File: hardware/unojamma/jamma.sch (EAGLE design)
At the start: 21 parts, among them T1 2N3904, T2 2N3904, T3 2N3904, X1 53048-09

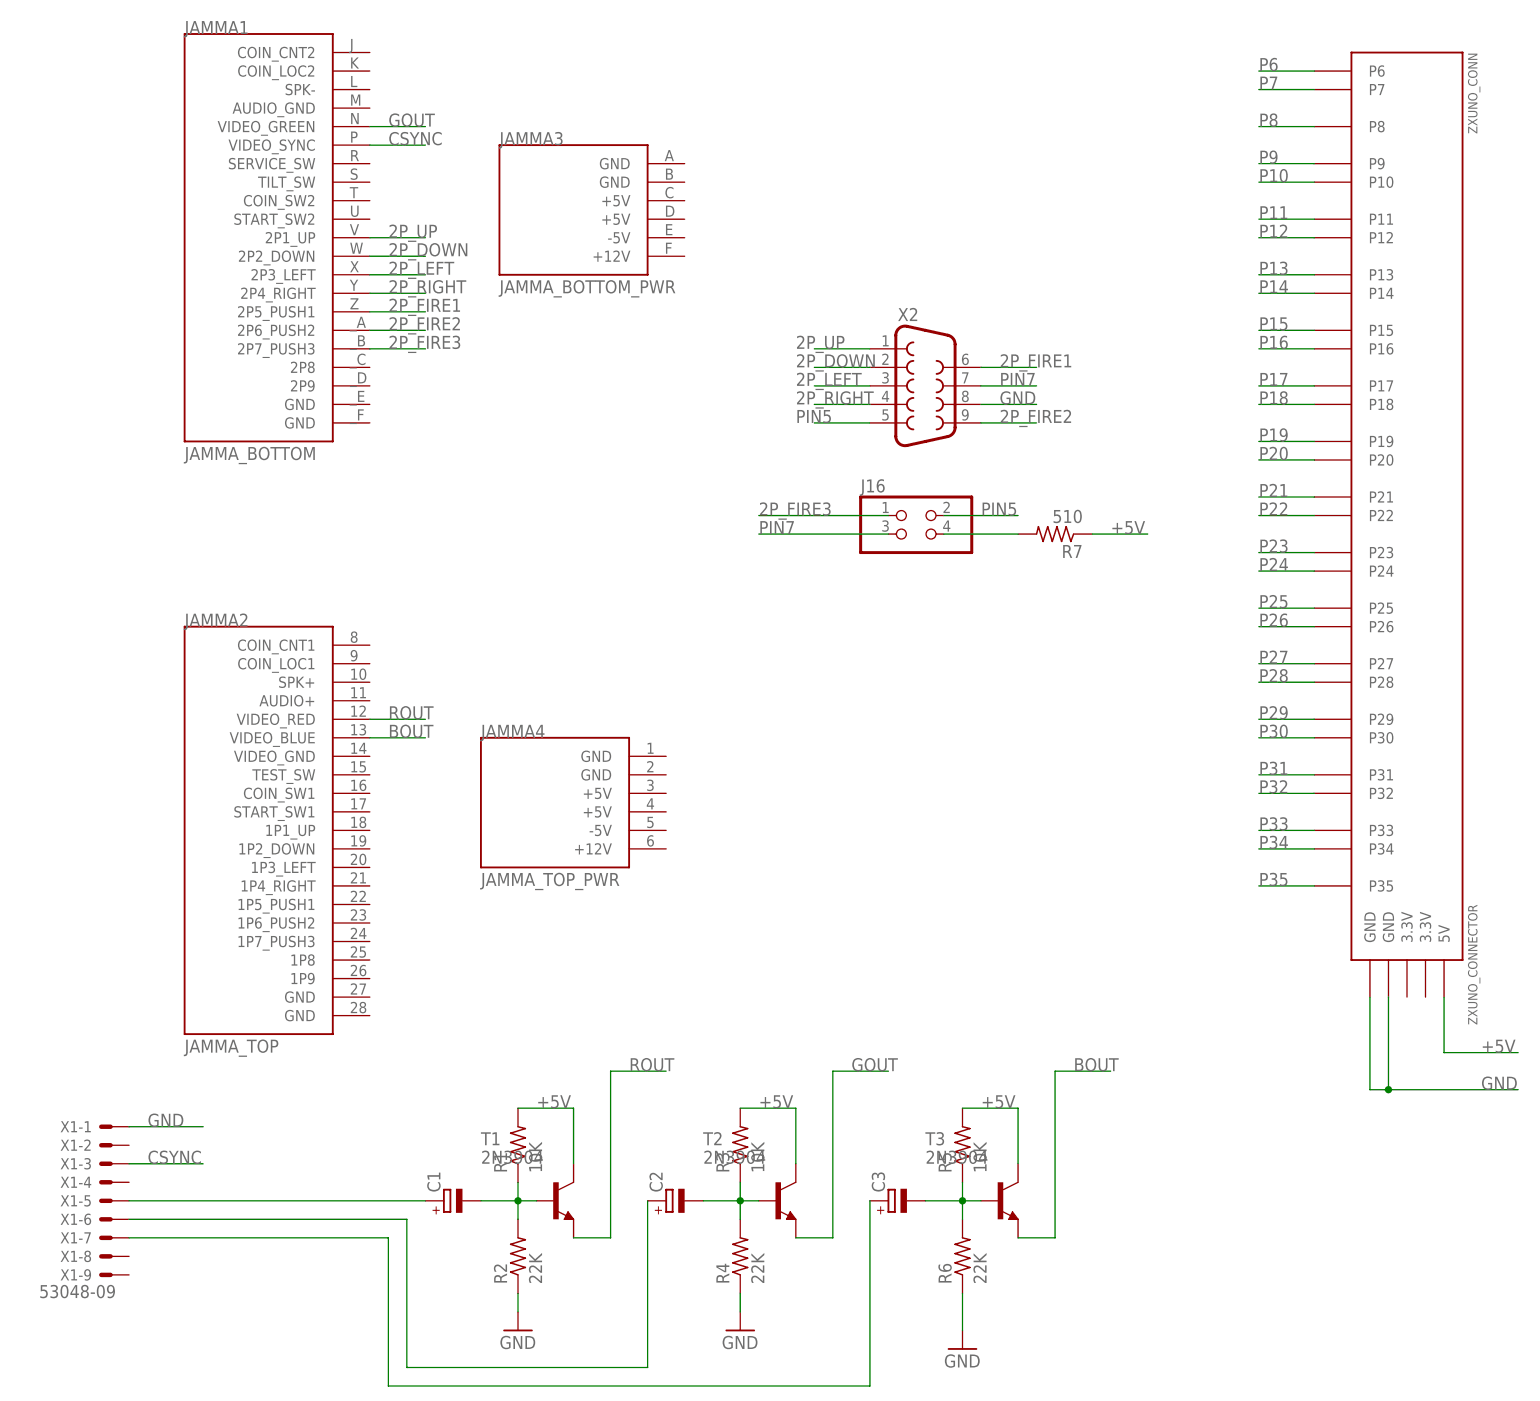
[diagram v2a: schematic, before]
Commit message: Añado amplificador de audio
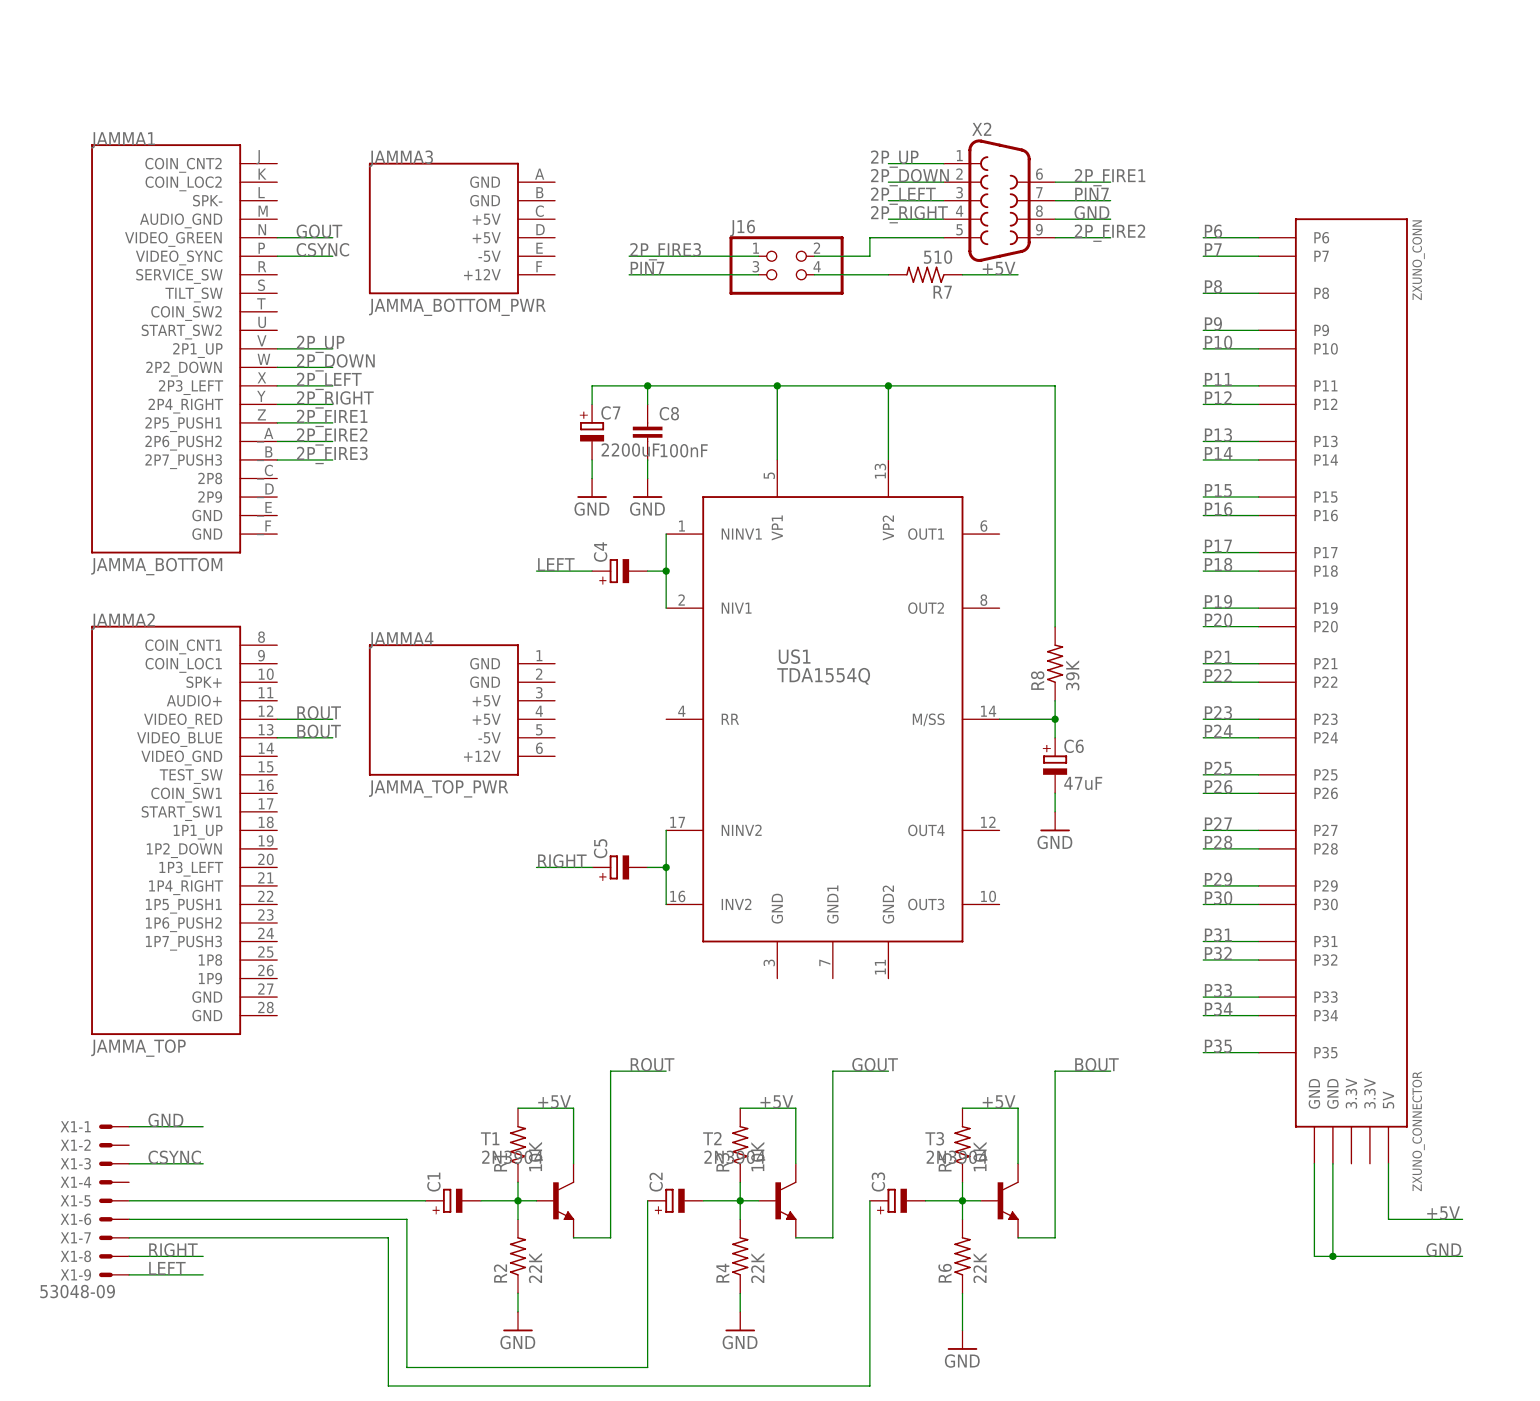
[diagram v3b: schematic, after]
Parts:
- added C4, C5: (no value), rcl:CPOL-EUE2-5
- added C6: 47uF, rcl:CPOL-EUE7.5-16
- added C7: 2200uF, rcl:CPOL-EUE5-10.5
- added C8: 100nF, rcl:C-EU025-025X050
- added R8: 39K, rcl:R-US_0204/7
- added US1: TDA1554Q, PowerAmplifier:TDA1554Q
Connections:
- net PIN5 renamed N$5
- new net LEFT: C4.+, X1-9.S
- new net N$1: C4.-, US1.NINV1, US1.NIV1
- new net N$2: C5.-, US1.INV2, US1.NINV2
- new net N$3: C7.+, C8.1, R8.2, US1.VP1, US1.VP2
- new net N$7: C6.+, R8.1, US1.M/SS
- new net RIGHT: C5.+, X1-8.S
- net GND: now also C6.-, C7.-, C8.2
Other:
- moved on the sheet: J16, JAMMA1, JAMMA2, JAMMA3, JAMMA4, R7, X2, ZXUNO_CONN

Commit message: Empiezo ruteado
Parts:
- added JP1: (no value), pinhead:PINHD-2X3/90
- added JP2, JP3: (no value), pinhead:PINHD-1X2
- added JP4, JP5: (no value), pinhead:PINHD-1X1
- added SW1: (no value), special:SW_DIP-8
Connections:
- removed net N$3: C7.+, C8.1, R8.2, US1.VP1, US1.VP2
- new net +12V: C7.+, C8.1, JP4.1, R8.2, US1.VP1, US1.VP2
- new net 1P_DOWN: JAMMA2.1P2_DOWN
- new net 1P_FIRE1: JAMMA2.1P5_PUSH1
- new net 1P_FIRE2: JAMMA2.1P6_PUSH2
- new net 1P_FIRE3: JAMMA2.1P7_PUSH3
- new net 1P_FIRE4: JAMMA2.1P8
- new net 1P_LEFT: JAMMA2.1P3_LEFT
- new net 1P_RIGHT: JAMMA2.1P4_RIGHT
- new net 1P_START: JAMMA2.START_SW1
- new net 1P_UP: JAMMA2.1P1_UP
- new net 2P_FIRE4: JAMMA1.2P8
- new net 2P_START: JAMMA1.START_SW2
- new net COIN1: JAMMA2.COIN_SW1
- new net COIN2: JAMMA1.COIN_SW2
- new net J+12V: JAMMA3.+12V, JAMMA4.+12V, JP5.1
- new net J+5V: JAMMA3.+5V@1, JAMMA3.+5V@2, JAMMA4.+5V@1, JAMMA4.+5V@2, JP3.2
- new net JGND: JAMMA3.GND@1, JAMMA3.GND@2, JAMMA4.GND@1, JAMMA4.GND@2, JP3.1
- new net SERVICE: JAMMA1.SERVICE_SW
- new net SPK1: JAMMA1.SPK-, JP1.4
- new net SPKL: JP1.2, US1.OUT4
- new net SPKR: JAMMA2.SPK+, US1.OUT1
- new net TEST: JP1.3
- new net TEST1: JAMMA1.AUDIO_GND, JP1.1
- new net TEST2: JAMMA2.TEST_SW, JP1.5
- net +5V: now also JP2.2
- net GND: now also JAMMA1.GND@3, JAMMA1.GND@4, JAMMA2.GND@3, JAMMA2.GND@4, JAMMA2.VIDEO_GND, JP1.6, JP2.1, SW1.10, SW1.11, SW1.12, SW1.13, SW1.14, SW1.15, SW1.16, SW1.9, US1.GND, US1.GND1, US1.GND2, US1.OUT2, US1.OUT3
- net LEFT: now also C5.+; no longer C4.+
- net RIGHT: now also C4.+; no longer C5.+
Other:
- moved on the sheet: C6, R8

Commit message: Más ruteado
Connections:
- removed net P32: ZXUNO_CONN.P32
- removed net P33: ZXUNO_CONN.P33
- removed net P34: ZXUNO_CONN.P34
- removed net P35: ZXUNO_CONN.P35
- removed net P6: ZXUNO_CONN.P6
- removed net P7: ZXUNO_CONN.P7
- removed net P8: ZXUNO_CONN.P8
- removed net P9: ZXUNO_CONN.P9
- net 1P_FIRE3: now also ZXUNO_CONN.P8
- net 1P_FIRE4: now also ZXUNO_CONN.P6
- net 2P_FIRE3: now also ZXUNO_CONN.P9
- net 2P_FIRE4: now also ZXUNO_CONN.P7
- net COIN1: now also ZXUNO_CONN.P33
- net COIN2: now also ZXUNO_CONN.P32
- net SERVICE: now also ZXUNO_CONN.P34
- net TEST: now also ZXUNO_CONN.P35

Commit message: Me faltan 16 líneas
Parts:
- removed C8: 100nF, rcl:C-EU025-025X050
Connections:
- removed net P16: ZXUNO_CONN.P16
- removed net P19: ZXUNO_CONN.P19
- removed net P22: ZXUNO_CONN.P22
- removed net P25: ZXUNO_CONN.P25
- removed net P28: ZXUNO_CONN.P28
- removed net P29: ZXUNO_CONN.P29
- removed net P30: ZXUNO_CONN.P30
- removed net P31: ZXUNO_CONN.P31
- new net SW1: SW1.8, ZXUNO_CONN.P34
- new net SW2: SW1.7, ZXUNO_CONN.P35
- new net SW3: SW1.6, ZXUNO_CONN.P31
- new net SW4: SW1.5, ZXUNO_CONN.P28
- new net SW5: SW1.4, ZXUNO_CONN.P25
- new net SW6: SW1.3, ZXUNO_CONN.P22
- new net SW7: SW1.2, ZXUNO_CONN.P19
- new net SW8: SW1.1, ZXUNO_CONN.P16
- net +12V: no longer C8.1
- net 1P_FIRE3: no longer ZXUNO_CONN.P8
- net 1P_FIRE4: no longer ZXUNO_CONN.P6
- net 1P_START: now also ZXUNO_CONN.P30
- net 2P_START: now also ZXUNO_CONN.P29
- net COIN1: now also ZXUNO_CONN.P32; no longer ZXUNO_CONN.P33
- net COIN2: now also ZXUNO_CONN.P6; no longer ZXUNO_CONN.P32
- net GND: no longer C8.2
- net SERVICE: now also ZXUNO_CONN.P8; no longer ZXUNO_CONN.P34
- net TEST: now also ZXUNO_CONN.P33; no longer ZXUNO_CONN.P35

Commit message: uno-jamma acabado
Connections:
- removed net P10: ZXUNO_CONN.P10
- removed net P11: ZXUNO_CONN.P11
- removed net P12: ZXUNO_CONN.P12
- removed net P13: ZXUNO_CONN.P13
- removed net P14: ZXUNO_CONN.P14
- removed net P15: ZXUNO_CONN.P15
- removed net P17: ZXUNO_CONN.P17
- removed net P18: ZXUNO_CONN.P18
- removed net P20: ZXUNO_CONN.P20
- removed net P21: ZXUNO_CONN.P21
- removed net P23: ZXUNO_CONN.P23
- removed net P24: ZXUNO_CONN.P24
- removed net P26: ZXUNO_CONN.P26
- removed net P27: ZXUNO_CONN.P27
- net 1P_DOWN: now also ZXUNO_CONN.P24
- net 1P_FIRE1: now also ZXUNO_CONN.P15
- net 1P_FIRE2: now also ZXUNO_CONN.P14
- net 1P_FIRE3: now also ZXUNO_CONN.P10
- net 1P_FIRE4: now also ZXUNO_CONN.P9
- net 1P_LEFT: now also ZXUNO_CONN.P21
- net 1P_RIGHT: now also ZXUNO_CONN.P18
- net 1P_UP: now also ZXUNO_CONN.P27
- net 2P_DOWN: now also ZXUNO_CONN.P23
- net 2P_FIRE1: now also ZXUNO_CONN.P13
- net 2P_FIRE2: now also ZXUNO_CONN.P12
- net 2P_FIRE3: now also ZXUNO_CONN.P11; no longer ZXUNO_CONN.P9
- net 2P_LEFT: now also ZXUNO_CONN.P20
- net 2P_RIGHT: now also ZXUNO_CONN.P17
- net 2P_UP: now also ZXUNO_CONN.P26
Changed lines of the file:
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@@
-</segment>
-</net>
-<net name="P10" class="0">
-<segment>
-<wire x1="154.94" y1="132.08" x2="162.56" y2="132.08" width="0.1524" layer="91"/>
-<label x="154.94" y="132.08" size="1.778" layer="95"/>
-<pinref part="ZXUNO_CONN" gate="G$1" pin="P10"/>
-</segment>
-</net>
-<net name="P11" class="0">
-<segment>
-<wire x1="154.94" y1="127" x2="162.56" y2="127" width="0.1524" layer="91"/>
-<label x="154.94" y="127" size="1.778" layer="95"/>
-<pinref part="ZXUNO_CONN" gate="G$1" pin="P11"/>
-</segment>
-</net>
-<net name="P12" class="0">
-<segment>
-<wire x1="154.94" y1="124.46" x2="162.56" y2="124.46" width="0.1524" layer="91"/>
-<label x="154.94" y="124.46" size="1.778" layer="95"/>
-<pinref part="ZXUNO_CONN" gate="G$1" pin="P12"/>
-</segment>
-</net>
-<net name="P13" class="0">
-<segment>
-<wire x1="154.94" y1="119.38" x2="162.56" y2="119.38" width="0.1524" layer="91"/>
-<label x="154.94" y="119.38" size="1.778" layer="95"/>
-<pinref part="ZXUNO_CONN" gate="G$1" pin="P13"/>
-</segment>
-</net>
-<net name="P14" class="0">
-<segment>
-<wire x1="154.94" y1="116.84" x2="162.56" y2="116.84" width="0.1524" layer="91"/>
-<label x="154.94" y="116.84" size="1.778" layer="95"/>
-<pinref part="ZXUNO_CONN" gate="G$1" pin="P14"/>
-</segment>
-</net>
-<net name="P15" class="0">
-<segment>
-<wire x1="154.94" y1="111.76" x2="162.56" y2="111.76" width="0.1524" layer="91"/>
-<label x="154.94" y="111.76" size="1.778" layer="95"/>
-<pinref part="ZXUNO_CONN" gate="G$1" pin="P15"/>
-</segment>
-</net>
-<net name="P17" class="0">
-<segment>
-<wire x1="154.94" y1="104.14" x2="162.56" y2="104.14" width="0.1524" layer="91"/>
-<label x="154.94" y="104.14" size="1.778" layer="95"/>
-<pinref part="ZXUNO_CONN" gate="G$1" pin="P17"/>
-</segment>
-</net>
-<net name="P18" class="0">
-<segment>
-<wire x1="154.94" y1="101.6" x2="162.56" y2="101.6" width="0.1524" layer="91"/>
-<label x="154.94" y="101.6" size="1.778" layer="95"/>
-<pinref part="ZXUNO_CONN" gate="G$1" pin="P18"/>
-</segment>
-</net>
-<net name="P20" class="0">
-<segment>
-<wire x1="154.94" y1="93.98" x2="162.56" y2="93.98" width="0.1524" layer="91"/>
-<label x="154.94" y="93.98" size="1.778" layer="95"/>
-<pinref part="ZXUNO_CONN" gate="G$1" pin="P20"/>
-</segment>
-</net>
-<net name="P21" class="0">
-<segment>
-<wire x1="154.94" y1="88.9" x2="162.56" y2="88.9" width="0.1524" layer="91"/>
-<label x="154.94" y="88.9" size="1.778" layer="95"/>
-<pinref part="ZXUNO_CONN" gate="G$1" pin="P21"/>
-</segment>
-</net>
-<net name="P23" class="0">
-<segment>
-<wire x1="154.94" y1="81.28" x2="162.56" y2="81.28" width="0.1524" layer="91"/>
-<label x="154.94" y="81.28" size="1.778" layer="95"/>
-<pinref part="ZXUNO_CONN" gate="G$1" pin="P23"/>
-</segment>
-</net>
-<net name="P24" class="0">
-<segment>
-<wire x1="154.94" y1="78.74" x2="162.56" y2="78.74" width="0.1524" layer="91"/>
-<label x="154.94" y="78.74" size="1.778" layer="95"/>
-<pinref part="ZXUNO_CONN" gate="G$1" pin="P24"/>
-</segment>
-</net>
-<net name="P26" class="0">
-<segment>
-<wire x1="154.94" y1="71.12" x2="162.56" y2="71.12" width="0.1524" layer="91"/>
-<label x="154.94" y="71.12" size="1.778" layer="95"/>
-<pinref part="ZXUNO_CONN" gate="G$1" pin="P26"/>
 </segment>
 </net>
@@
 <label x="109.22" y="157.48" size="1.778" layer="95"/>
 </segment>
+<segment>
+<wire x1="154.94" y1="71.12" x2="162.56" y2="71.12" width="0.1524" layer="91"/>
+<label x="154.94" y="71.12" size="1.778" layer="95"/>
+<pinref part="ZXUNO_CONN" gate="G$1" pin="P26"/>
+</segment>
 </net>
 <net name="2P_DOWN" class="0">
@@
 <label x="109.22" y="154.94" size="1.778" layer="95"/>
 </segment>
+<segment>
+<wire x1="154.94" y1="81.28" x2="162.56" y2="81.28" width="0.1524" layer="91"/>
+<label x="154.94" y="81.28" size="1.778" layer="95"/>
+<pinref part="ZXUNO_CONN" gate="G$1" pin="P23"/>
+</segment>
 </net>
 <net name="2P_LEFT" class="0">
@@
 <label x="109.22" y="152.4" size="1.778" layer="95"/>
 </segment>
+<segment>
+<wire x1="154.94" y1="93.98" x2="162.56" y2="93.98" width="0.1524" layer="91"/>
+<label x="154.94" y="93.98" size="1.778" layer="95"/>
+<pinref part="ZXUNO_CONN" gate="G$1" pin="P20"/>
+</segment>
 </net>
 <net name="2P_RIGHT" class="0">
@@
 <label x="109.22" y="149.86" size="1.778" layer="95"/>
 </segment>
+<segment>
+<wire x1="154.94" y1="104.14" x2="162.56" y2="104.14" width="0.1524" layer="91"/>
+<label x="154.94" y="104.14" size="1.778" layer="95"/>
+<pinref part="ZXUNO_CONN" gate="G$1" pin="P17"/>
+</segment>
 </net>
 <net name="2P_FIRE1" class="0">
@@
 <label x="137.16" y="154.94" size="1.778" layer="95"/>
 </segment>
+<segment>
+<wire x1="154.94" y1="119.38" x2="162.56" y2="119.38" width="0.1524" layer="91"/>
+<label x="154.94" y="119.38" size="1.778" layer="95"/>
+<pinref part="ZXUNO_CONN" gate="G$1" pin="P13"/>
+</segment>
 </net>
 <net name="2P_FIRE2" class="0">
@@
 <label x="137.16" y="147.32" size="1.778" layer="95"/>
 </segment>
+<segment>
+<wire x1="154.94" y1="124.46" x2="162.56" y2="124.46" width="0.1524" layer="91"/>
+<label x="154.94" y="124.46" size="1.778" layer="95"/>
+<pinref part="ZXUNO_CONN" gate="G$1" pin="P12"/>
+</segment>
 </net>
 <net name="2P_FIRE3" class="0">
@@
 </segment>
 <segment>
-<wire x1="154.94" y1="134.62" x2="162.56" y2="134.62" width="0.1524" layer="91"/>
-<label x="154.94" y="134.62" size="1.778" layer="95"/>
-<pinref part="ZXUNO_CONN" gate="G$1" pin="P9"/>
+<wire x1="154.94" y1="127" x2="162.56" y2="127" width="0.1524" layer="91"/>
+<label x="154.94" y="127" size="1.778" layer="95"/>
+<pinref part="ZXUNO_CONN" gate="G$1" pin="P11"/>
 </segment>
 </net>
@@
 <label x="30.48" y="66.04" size="1.778" layer="95"/>
 </segment>
+<segment>
+<wire x1="154.94" y1="66.04" x2="162.56" y2="66.04" width="0.1524" layer="91"/>
+<label x="154.94" y="66.04" size="1.778" layer="95"/>
+<pinref part="ZXUNO_CONN" gate="G$1" pin="P27"/>
+</segment>
 </net>
 <net name="1P_DOWN" class="0">
@@
 <label x="30.48" y="63.5" size="1.778" layer="95"/>
 </segment>
+<segment>
+<wire x1="154.94" y1="78.74" x2="162.56" y2="78.74" width="0.1524" layer="91"/>
+<label x="154.94" y="78.74" size="1.778" layer="95"/>
+<pinref part="ZXUNO_CONN" gate="G$1" pin="P24"/>
+</segment>
 </net>
 <net name="1P_LEFT" class="0">
@@
 <label x="30.48" y="60.96" size="1.778" layer="95"/>
 </segment>
+<segment>
+<wire x1="154.94" y1="88.9" x2="162.56" y2="88.9" width="0.1524" layer="91"/>
+<label x="154.94" y="88.9" size="1.778" layer="95"/>
+<pinref part="ZXUNO_CONN" gate="G$1" pin="P21"/>
+</segment>
 </net>
 <net name="1P_RIGHT" class="0">
@@
 <label x="30.48" y="58.42" size="1.778" layer="95"/>
 </segment>
+<segment>
+<wire x1="154.94" y1="101.6" x2="162.56" y2="101.6" width="0.1524" layer="91"/>
+<label x="154.94" y="101.6" size="1.778" layer="95"/>
+<pinref part="ZXUNO_CONN" gate="G$1" pin="P18"/>
+</segment>
 </net>
 <net name="1P_FIRE1" class="0">
@@
 <label x="30.48" y="55.88" size="1.778" layer="95"/>
 </segment>
+<segment>
+<wire x1="154.94" y1="111.76" x2="162.56" y2="111.76" width="0.1524" layer="91"/>
+<label x="154.94" y="111.76" size="1.778" layer="95"/>
+<pinref part="ZXUNO_CONN" gate="G$1" pin="P15"/>
+</segment>
 </net>
 <net name="1P_FIRE2" class="0">
@@
 <label x="30.48" y="53.34" size="1.778" layer="95"/>
 </segment>
+<segment>
+<wire x1="154.94" y1="116.84" x2="162.56" y2="116.84" width="0.1524" layer="91"/>
+<label x="154.94" y="116.84" size="1.778" layer="95"/>
+<pinref part="ZXUNO_CONN" gate="G$1" pin="P14"/>
+</segment>
 </net>
 <net name="1P_FIRE3" class="0">
@@
 <label x="30.48" y="50.8" size="1.778" layer="95"/>
 </segment>
+<segment>
+<wire x1="154.94" y1="132.08" x2="162.56" y2="132.08" width="0.1524" layer="91"/>
+<label x="154.94" y="132.08" size="1.778" layer="95"/>
+<pinref part="ZXUNO_CONN" gate="G$1" pin="P10"/>
+</segment>
 </net>
 <net name="1P_FIRE4" class="0">
@@
 <label x="30.48" y="48.26" size="1.778" layer="95"/>
 </segment>
+<segment>
+<wire x1="154.94" y1="134.62" x2="162.56" y2="134.62" width="0.1524" layer="91"/>
+<label x="154.94" y="134.62" size="1.778" layer="95"/>
+<pinref part="ZXUNO_CONN" gate="G$1" pin="P9"/>
+</segment>
 </net>
 <net name="JGND" class="1">
@@
 </segment>
 </net>
-<net name="P27" class="0">
-<segment>
-<wire x1="154.94" y1="66.04" x2="162.56" y2="66.04" width="0.1524" layer="91"/>
-<label x="154.94" y="66.04" size="1.778" layer="95"/>
-<pinref part="ZXUNO_CONN" gate="G$1" pin="P27"/>
-</segment>
-</net>
